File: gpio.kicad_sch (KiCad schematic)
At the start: 19 parts, among them Q1 AUIRF7316QTR, Q2 AUIRF7316QTR, Q3 AUIRF7316QTR, Q4 AUIRF7316QTR, U10 PCF8574DWR, U8 NPIC6C596ADJ

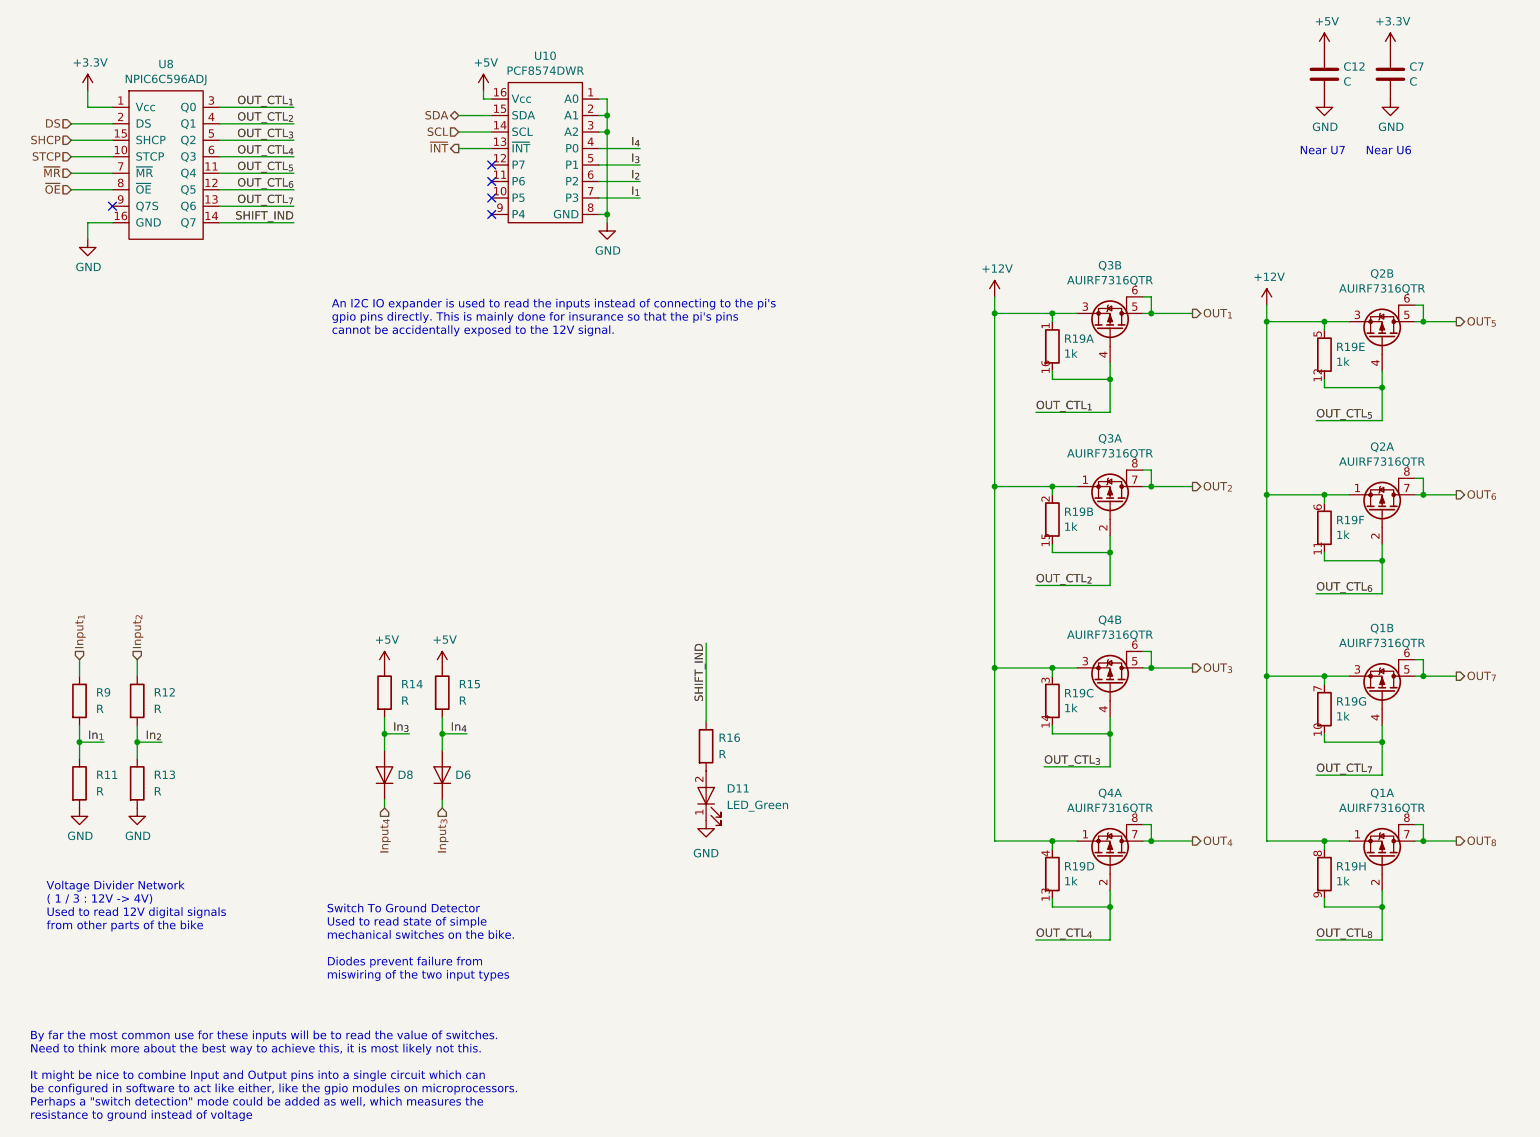
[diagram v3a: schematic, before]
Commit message: components group and placed in roughly the right position
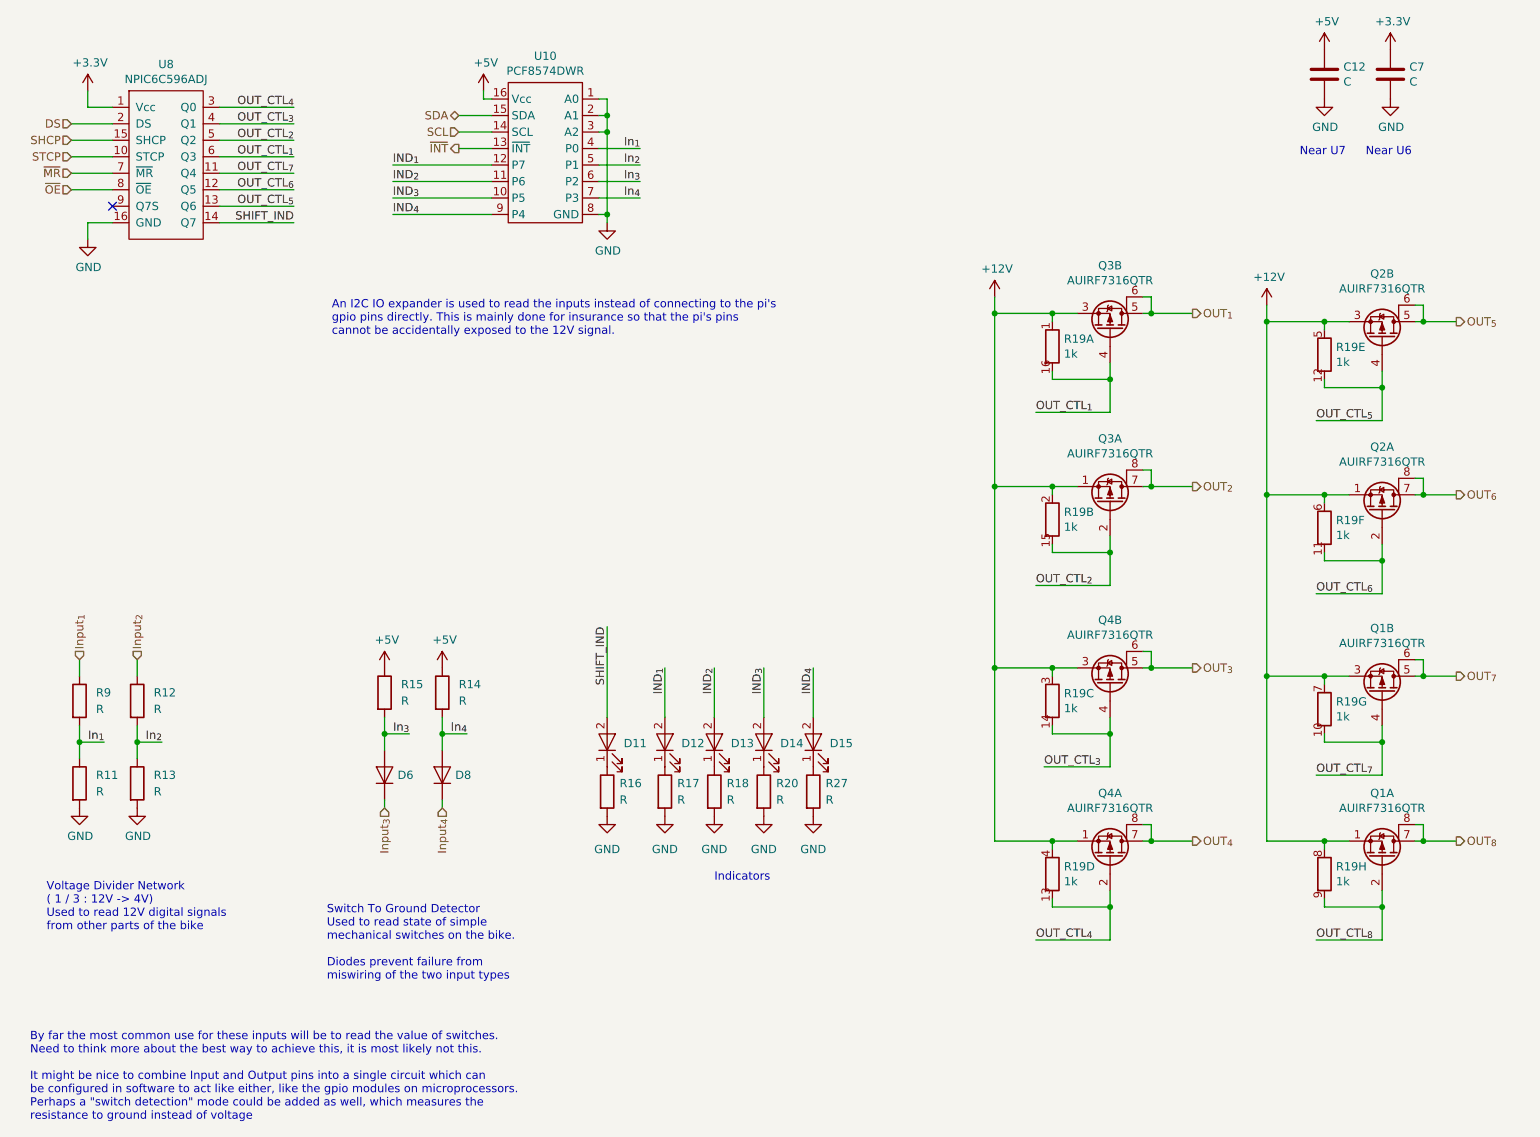
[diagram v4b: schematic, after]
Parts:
- added D12, D13, D14, D15: LED_Green, LED_SMD:LED_0805_2012Metric_Pad1.15x1.40mm_HandSolder, symbol ecafe-racer:LED_Green
- added R17, R18, R20, R27: R, Resistor_SMD:R_0805_2012Metric, symbol Device:R
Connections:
- net I_{1} is gone; now on net In_{4}: U10.7 (P3)
- net I_{2} is gone; now on net In_{3}: U10.6 (P2)
- net I_{3} is gone; now on net In_{2}: U10.5 (P1)
- net I_{4} is gone; now on net In_{1}: U10.4 (P0)
- net GND: now also R16.2, R17.2, R18.2, R20.2, R27.2; no longer D11.1
- net In_{3}: now also D6.2 (A), R15.2; no longer D8.2 (A), R14.2
- net In_{4}: now also D8.2 (A), R14.2; no longer D6.2 (A), R15.2
- net OUT_CTL_{1}: now also U8.6 (Q3); no longer U8.3 (Q0)
- net OUT_CTL_{2}: now also U8.5 (Q2); no longer U8.4 (Q1)
- net OUT_CTL_{3}: now also U8.4 (Q1); no longer U8.5 (Q2)
- net OUT_CTL_{4}: now also U8.3 (Q0); no longer U8.6 (Q3)
- net OUT_CTL_{5}: now also U8.13 (Q6); no longer U8.11 (Q4)
- net OUT_CTL_{7}: now also U8.11 (Q4); no longer U8.13 (Q6)
- net SHIFT_IND: now also D11.2; no longer R16.1
- net IND_{3}: now reaches U10.10 (P5)
- net IND_{3}: now also D14.2
- net IND_{2}: now reaches U10.11 (P6)
- net IND_{2}: now also D13.2
- net IND_{1}: now reaches U10.12 (P7)
- net IND_{1}: now also D12.2
- net IND_{4}: now reaches U10.9 (P4)
- net IND_{4}: now also D15.2
- new net: D13.1, R18.1
- new net: D12.1, R17.1
- new net: D14.1, R20.1
- new net: D15.1, R27.1
- new net: D11.1, R16.1
- no-connect marks 5 -> 1
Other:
- note added: "Indicators"
- moved on the sheet: D11, D6, D8, R14, R15, R16

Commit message: WIP
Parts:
- added D17: LED_Green, LED_SMD:LED_0805_2012Metric_Pad1.15x1.40mm_HandSolder, symbol ecafe-racer:LED_Green
- added R29: R, Resistor_SMD:R_0805_2012Metric, symbol Device:R
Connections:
- net OUT_CTL_{8} is gone; now on net OUT_CTL_{7}: Q1.2 (G1), R19.9
- net GND: now also R29.2
- net OUT_{8} renamed OUT_IND
- net OUT_IND: now also D17.2
- new net: D17.1, R29.1
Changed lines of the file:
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@@
     (stroke (width 0) (type solid) (color 0 0 0 0))
   )
-  (wire (pts (xy 124.46 123.19) (xy 124.46 130.81))
-    (stroke (width 0) (type solid) (color 0 0 0 0))
-  )
-  (wire (pts (xy 132.08 123.19) (xy 132.08 130.81))
-    (stroke (width 0) (type solid) (color 0 0 0 0))
-  )
-  (wire (pts (xy 139.7 123.19) (xy 139.7 130.81))
-    (stroke (width 0) (type solid) (color 0 0 0 0))
-  )
-  (wire (pts (xy 147.32 123.19) (xy 147.32 130.81))
+  (wire (pts (xy 124.46 121.92) (xy 124.46 130.81))
+    (stroke (width 0) (type solid) (color 0 0 0 0))
+  )
+  (wire (pts (xy 132.08 121.92) (xy 132.08 130.81))
+    (stroke (width 0) (type solid) (color 0 0 0 0))
+  )
+  (wire (pts (xy 139.7 121.92) (xy 139.7 130.81))
+    (stroke (width 0) (type solid) (color 0 0 0 0))
+  )
+  (wire (pts (xy 147.32 121.92) (xy 147.32 130.81))
+    (stroke (width 0) (type solid) (color 0 0 0 0))
+  )
+  (wire (pts (xy 157.48 121.92) (xy 157.48 130.81))
     (stroke (width 0) (type solid) (color 0 0 0 0))
   )
@@
     (stroke (width 0) (type solid) (color 0 0 0 0))
   )
-  (wire (pts (xy 241.3 149.86) (xy 246.38 149.86))
+  (wire (pts (xy 241.3 149.86) (xy 254 149.86))
     (stroke (width 0) (type solid) (color 0 0 0 0))
   )
@@
     (effects (font (size 1.27 1.27)) (justify right bottom))
   )
-  (label "IND_{1}" (at 124.46 123.19 270)
-    (effects (font (size 1.27 1.27)) (justify right bottom))
-  )
-  (label "IND_{2}" (at 132.08 123.19 270)
-    (effects (font (size 1.27 1.27)) (justify right bottom))
-  )
-  (label "IND_{3}" (at 139.7 123.19 270)
-    (effects (font (size 1.27 1.27)) (justify right bottom))
-  )
-  (label "IND_{4}" (at 147.32 123.19 270)
+  (label "IND_{1}" (at 124.46 121.92 270)
+    (effects (font (size 1.27 1.27)) (justify right bottom))
+  )
+  (label "IND_{2}" (at 132.08 121.92 270)
+    (effects (font (size 1.27 1.27)) (justify right bottom))
+  )
+  (label "IND_{3}" (at 139.7 121.92 270)
+    (effects (font (size 1.27 1.27)) (justify right bottom))
+  )
+  (label "IND_{4}" (at 147.32 121.92 270)
+    (effects (font (size 1.27 1.27)) (justify right bottom))
+  )
+  (label "OUT_IND" (at 157.48 121.92 270)
     (effects (font (size 1.27 1.27)) (justify right bottom))
   )
@@
     (effects (font (size 1.27 1.27)) (justify left bottom))
   )
-  (label "OUT_CTL_{8}" (at 224.79 165.1 0)
-    (effects (font (size 1.27 1.27)) (justify left bottom))
+  (label "OUT_CTL_{7}" (at 224.79 165.1 0)
+    (effects (font (size 1.27 1.27)) (justify left bottom))
+  )
+  (label "OUT_IND" (at 254 149.86 180)
+    (effects (font (size 1.27 1.27)) (justify right bottom))
   )
   (hierarchical_label "DS" (shape input) (at 33.02 39.37 180)
@@
     (effects (font (size 1.27 1.27)) (justify left))
   )
-  (hierarchical_label "OUT_{8}" (shape output) (at 246.38 149.86 0)
-    (effects (font (size 1.27 1.27)) (justify left))
-  )
   (symbol (lib_id "power:+3.3V") (at 35.56 34.29 0) (unit 1)
     (in_bom yes) (on_board yes)
@@
     (pin "1")
   )
+  (symbol (lib_id "power:GND") (at 157.48 146.05 0) (unit 1)
+    (in_bom yes) (on_board yes) (fields_autoplaced)
+    (property "Reference" "#PWR0145" (id 0) (at 157.48 152.4 0)
+      (effects (font (size 1.27 1.27)) hide)
+    )
+    (property "Value" "GND" (id 1) (at 157.48 151.13 0))
+    (property "Footprint" "" (id 2) (at 157.48 146.05 0)
+      (effects (font (size 1.27 1.27)) hide)
+    )
+    (property "Datasheet" "" (id 3) (at 157.48 146.05 0)
+      (effects (font (size 1.27 1.27)) hide)
+    )
+    (pin "1")
+  )
   (symbol (lib_id "power:GND") (at 226.06 35.56 0) (unit 1)
     (in_bom yes) (on_board yes)
@@
     (pin "2")
   )
+  (symbol (lib_id "Device:R") (at 157.48 142.24 0) (unit 1)
+    (in_bom yes) (on_board yes) (fields_autoplaced)
+    (property "Reference" "R29" (id 0) (at 159.385 140.9699 0)
+      (effects (font (size 1.27 1.27)) (justify left))
+    )
+    (property "Value" "R" (id 1) (at 159.385 143.5099 0)
+      (effects (font (size 1.27 1.27)) (justify left))
+    )
+    (property "Footprint" "Resistor_SMD:R_0805_2012Metric" (id 2) (at 155.702 142.24 90)
+      (effects (font (size 1.27 1.27)) hide)
+    )
+    (property "Datasheet" "~" (id 3) (at 157.48 142.24 0)
+      (effects (font (size 1.27 1.27)) hide)
+    )
+    (pin "1")
+    (pin "2")
+  )
   (symbol (lib_name "symbols:CTS-766161102GP_18") (lib_id "symbols:CTS-766161102GP") (at 184.15 73.66 0) (unit 1)
     (in_bom yes) (on_board yes)
@@
       (effects (font (size 1.27 1.27)) hide)
     )
+    (pin "1")
+    (pin "2")
+  )
+  (symbol (lib_id "ecafe-racer:LED_Green") (at 157.48 134.62 90) (unit 1)
+    (in_bom yes) (on_board yes)
+    (property "Reference" "D17" (id 0) (at 160.02 134.8104 90)
+      (effects (font (size 1.27 1.27)) (justify right))
+    )
+    (property "Value" "LED_Green" (id 1) (at 160.655 136.0804 90)
+      (effects (font (size 1.27 1.27)) (justify right) hide)
+    )
+    (property "Footprint" "LED_SMD:LED_0805_2012Metric_Pad1.15x1.40mm_HandSolder" (id 2) (at 146.05 125.73 0)
+      (effects (font (size 1.27 1.27)) hide)
+    )
+    (property "Datasheet" "https://vcclite.com/wp-content/uploads/wpallimport/files/files/CMD1721Seriesver3.pdf" (id 3) (at 153.67 130.81 0)
+      (effects (font (size 1.27 1.27)) hide)
+    )
+    (property "Vendor" "Digikey" (id 4) (at 138.43 152.4 0)
+      (effects (font (size 1.27 1.27)) hide)
+    )
+    (property "Vendor Part" "L62405CT-ND" (id 5) (at 140.97 148.59 0)
+      (effects (font (size 1.27 1.27)) hide)
+    )
+    (property "Manufacturer" "Visual Communications Company - VCC" (id 6) (at 148.59 135.89 0)
+      (effects (font (size 1.27 1.27)) hide)
+    )
+    (property "Manufacturer Part" "CMD17-21VGC/TR8" (id 7) (at 143.51 146.05 0)
+      (effects (font (size 1.27 1.27)) hide)
+    )

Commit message: WIP
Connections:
- net IND_{1}: now also D15.2; no longer D12.2
- net IND_{2}: now also D12.2; no longer D13.2
- net IND_{3}: now also D13.2; no longer D14.2
- net IND_{4}: now also D14.2; no longer D15.2
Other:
- moved on the sheet: D12, D13, D14, D15, R17, R18, R20, R27
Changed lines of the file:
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@@
   (symbol (lib_id "Device:R") (at 124.46 142.24 0) (unit 1)
     (in_bom yes) (on_board yes) (fields_autoplaced)
-    (property "Reference" "R17" (id 0) (at 126.365 140.9699 0)
+    (property "Reference" "R27" (id 0) (at 126.365 140.9699 0)
       (effects (font (size 1.27 1.27)) (justify left))
     )
@@
   (symbol (lib_id "Device:R") (at 132.08 142.24 0) (unit 1)
     (in_bom yes) (on_board yes) (fields_autoplaced)
-    (property "Reference" "R18" (id 0) (at 133.985 140.9699 0)
+    (property "Reference" "R17" (id 0) (at 133.985 140.9699 0)
       (effects (font (size 1.27 1.27)) (justify left))
     )
@@
   (symbol (lib_id "Device:R") (at 139.7 142.24 0) (unit 1)
     (in_bom yes) (on_board yes) (fields_autoplaced)
-    (property "Reference" "R20" (id 0) (at 141.605 140.9699 0)
+    (property "Reference" "R18" (id 0) (at 141.605 140.9699 0)
       (effects (font (size 1.27 1.27)) (justify left))
     )
@@
   (symbol (lib_id "Device:R") (at 147.32 142.24 0) (unit 1)
     (in_bom yes) (on_board yes) (fields_autoplaced)
-    (property "Reference" "R27" (id 0) (at 149.225 140.9699 0)
+    (property "Reference" "R20" (id 0) (at 149.225 140.9699 0)
       (effects (font (size 1.27 1.27)) (justify left))
     )
@@
   (symbol (lib_id "ecafe-racer:LED_Green") (at 124.46 134.62 90) (unit 1)
     (in_bom yes) (on_board yes)
-    (property "Reference" "D12" (id 0) (at 127 134.8104 90)
+    (property "Reference" "D15" (id 0) (at 127 134.8104 90)
       (effects (font (size 1.27 1.27)) (justify right))
     )
@@
   (symbol (lib_id "ecafe-racer:LED_Green") (at 132.08 134.62 90) (unit 1)
     (in_bom yes) (on_board yes)
-    (property "Reference" "D13" (id 0) (at 134.62 134.8104 90)
+    (property "Reference" "D12" (id 0) (at 134.62 134.8104 90)
       (effects (font (size 1.27 1.27)) (justify right))
     )
@@
   (symbol (lib_id "ecafe-racer:LED_Green") (at 139.7 134.62 90) (unit 1)
     (in_bom yes) (on_board yes)
-    (property "Reference" "D14" (id 0) (at 142.24 134.8104 90)
+    (property "Reference" "D13" (id 0) (at 142.24 134.8104 90)
       (effects (font (size 1.27 1.27)) (justify right))
     )
@@
   (symbol (lib_id "ecafe-racer:LED_Green") (at 147.32 134.62 90) (unit 1)
     (in_bom yes) (on_board yes)
-    (property "Reference" "D15" (id 0) (at 149.86 134.8104 90)
-      (effects (font (size 1.27 1.27)) (justify right))
-    )
+    (property "Reference" "D14" (id 0) (at 149.86 134.8104 90)
+      (effects (font (size 1.27 1.27)) (justify right))
+    )

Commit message: geographical reannotate
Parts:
- renumbered C7 to C10, D15 to D11, D14 to D12, D17 to D13, D13 to D14, D12 to D15, D6 to D19, D8 to D20, D11 to D8, Q2 to Q4, Q4 to Q5, Q3 to Q6, Q1 to Q7, R9 to R14, R12 to R15, R17 to R24, R29 to R25, R27 to R26, R20 to R27, R18 to R28, R16 to R29, R15 to R30, R14 to R31, R13 to R32, R11 to R34, R19 to R35, U8 to U7, U10 to U9
